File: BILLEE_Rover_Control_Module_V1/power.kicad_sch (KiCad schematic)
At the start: 12 parts, among them CN1 LOGIC_PWR_XT60, U10 LT8612EUDE#TRPBF, U11 LT8612EUDE#TRPBF, U12 JETSON_PWR, U13 JETSON_PWR, U14 JETSON_PWR, U5 INA780BIDEKR, U6 TPS1HA08BQPWPRQ1, U7 TPS1HA08BQPWPRQ1, U8 TPS1HA08BQPWPRQ1, U9 LT8612EUDE#TRPBF

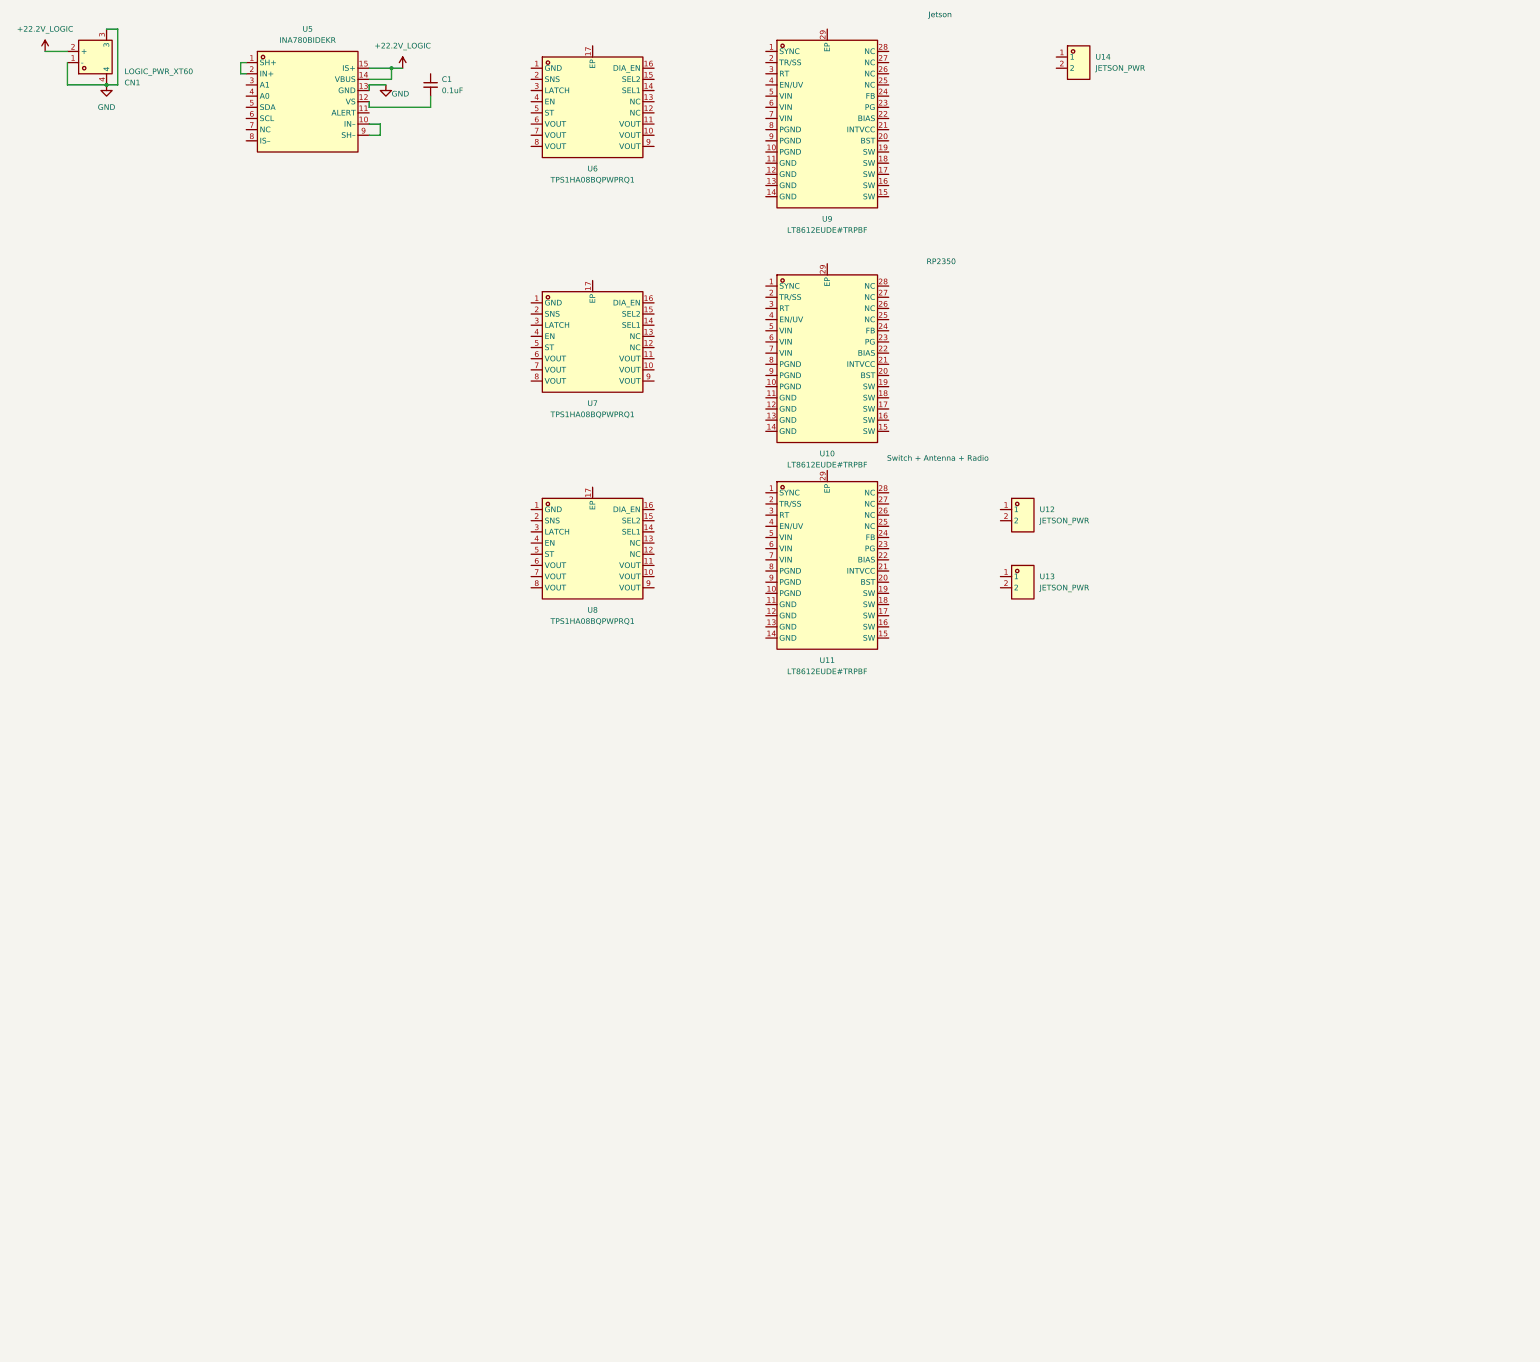
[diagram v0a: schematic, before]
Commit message: Implemented Logic Subsystem
Implemented all of the Logic subsystem, missing reverse circuit protection.
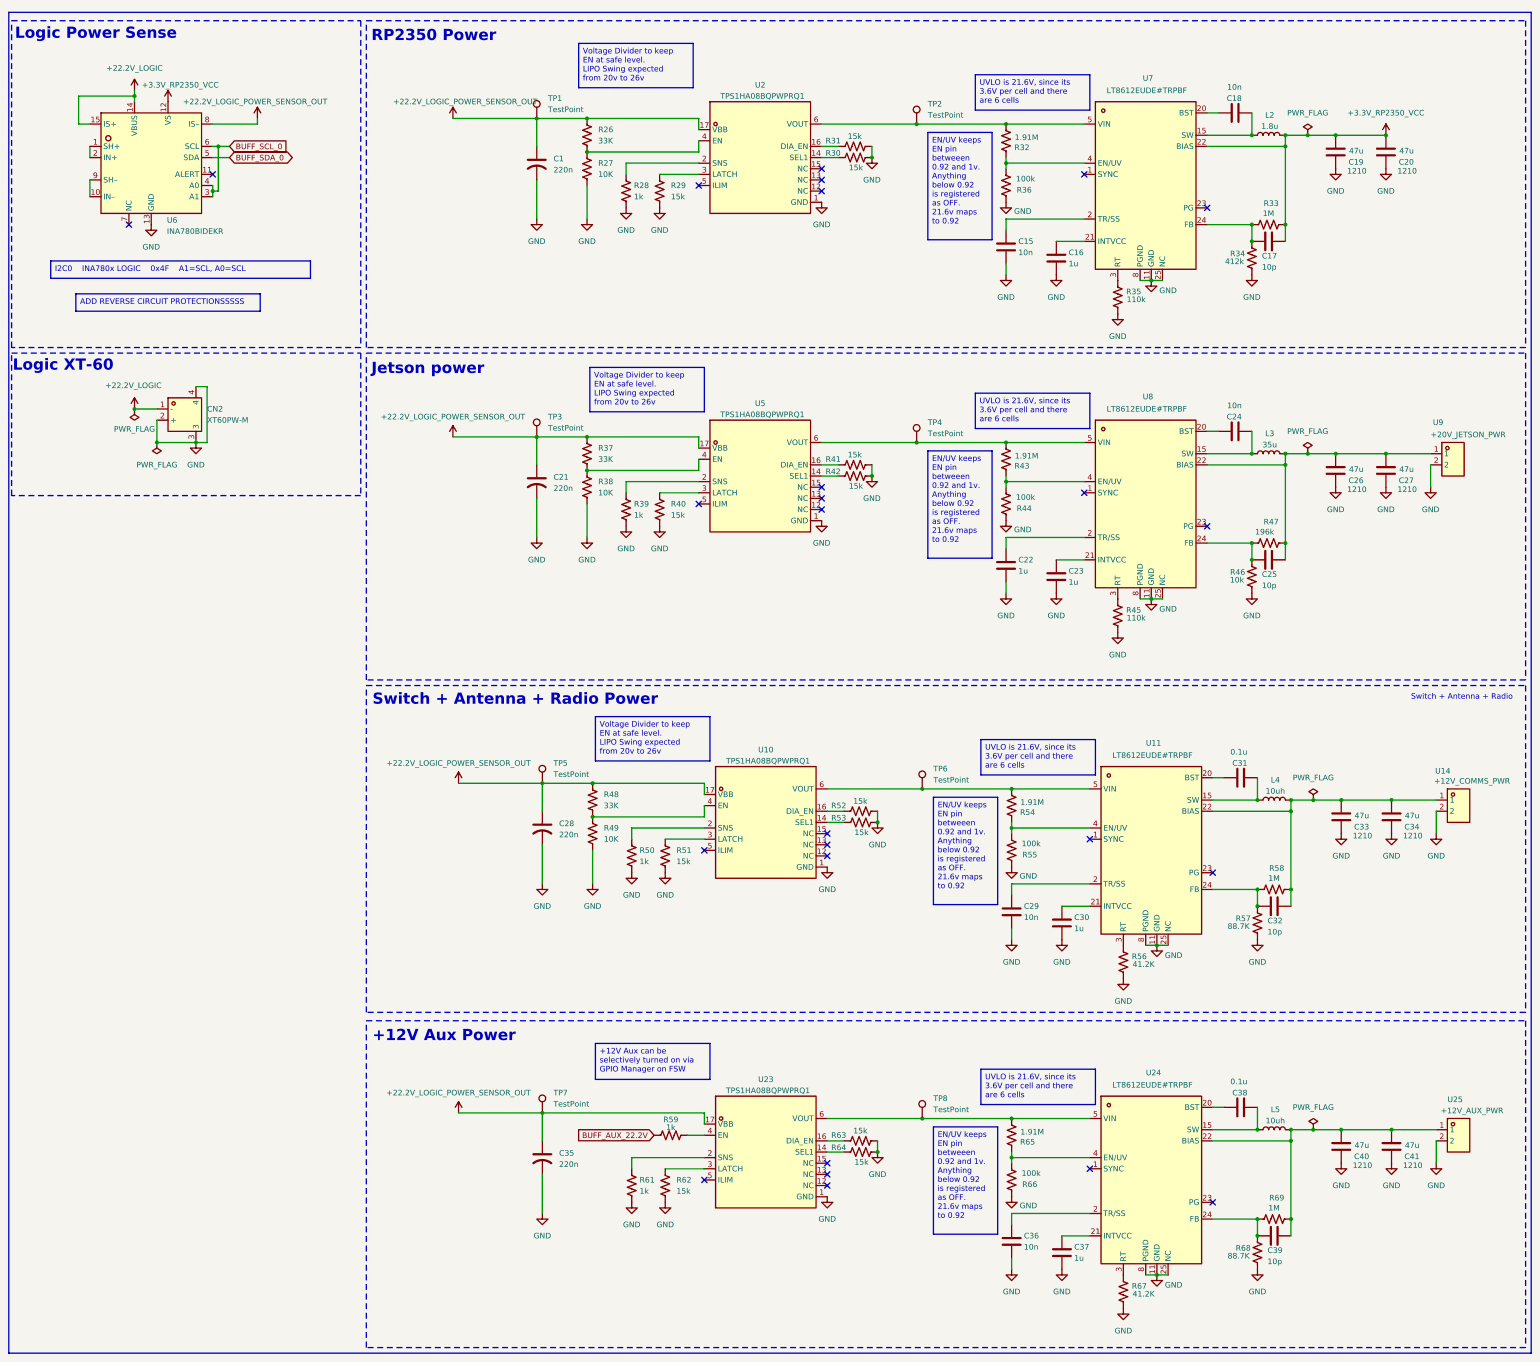
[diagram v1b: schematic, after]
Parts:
- removed C1: 0.1uF, symbol Device:C_Small
- removed CN1: LOGIC_PWR_XT60, PDB_LCSC:CONN-TH_XT60PW-M, symbol PDB_LSCS_Libs:XT60PW-M
- removed U10, U11, U9: LT8612EUDE#TRPBF, PDB_LCSC:QFN-28_L6.0-W3.0-P0.50-BL-EP, symbol PDB_LSCS_Libs:LT8612EUDE#TRPBF
- removed U12, U13, U14: JETSON_PWR, PDB_LCSC:CONN-TH_P5.00_KF301-5.0-2P, symbol PDB_LSCS_Libs:KF301-5.0-2P
- removed U5: INA780BIDEKR, PDB_LCSC:VQFN-15_L6.0-W6.0-P0.60-TL, symbol PDB_LSCS_Libs:INA780BIDEKR
- removed U6, U7, U8: TPS1HA08BQPWPRQ1, PDB_LCSC:HTSSOP-16_L5.0-W4.4-P0.65-LS6.4-BL-EP, symbol PDB_LSCS_Libs:TPS1HA08BQPWPRQ1
- added C1, C21, C28, C35: 220n, symbol Device:C_US
- added C15, C18, C24, C29, C36: 10n, symbol Device:C
- added C16, C22, C23, C30, C37: 1u, symbol Device:C
- added C17, C25, C32, C39: 10p, symbol Device:C
- added C19, C20, C26, C27, C33, C34, C40, C41: 47u, symbol Device:C
- added C31, C38: 0.1u, symbol Device:C
- added CN2: XT60PW-M, PDB_LCSC:CONN-TH_XT60PW-M, symbol PDB_LCSC_Libs:XT60PW-M
- added L2: 1.8u, symbol Device:L
- added L3: 35u, symbol Device:L
- added L4, L5: 10uh, symbol Device:L
- added R26, R37, R48: 33K, symbol Device:R_US
- added R27, R38, R49: 10K, symbol Device:R_US
- added R28, R39, R50, R59, R61: 1k, symbol Device:R_US
- added R29, R30, R31, R40, R41, R42, R51, R52, R53, R62, R63, R64: 15k, symbol Device:R_US
- added R32, R43, R54, R65: 1.91M, symbol Device:R_US
- added R33, R58, R69: 1M, symbol Device:R_US
- added R34: 412k, symbol Device:R_US
- added R35, R45: 110k, symbol Device:R_US
- added R36, R44, R55, R66: 100k, symbol Device:R_US
- added R46: 10k, symbol Device:R_US
- added R47: 196k, symbol Device:R_US
- added R56, R67: 41.2K, symbol Device:R_US
- added R57, R68: 88.7K, symbol Device:R_US
- added TP1, TP2, TP3, TP4, TP5, TP6, TP7, TP8: TestPoint, Connector_Pin:Pin_D1.0mm_L10.0mm, symbol Connector:TestPoint
- added U10, U2, U23, U5: TPS1HA08BQPWPRQ1, PDB_LCSC:HTSSOP-16_L5.0-W4.4-P0.65-LS6.4-BL-EP, symbol PDB_LCSC_Libs:TPS1HA08BQPWPRQ1
- added U11, U24, U7, U8: LT8612EUDE#TRPBF, PDB_LCSC:QFN-28_L6.0-W3.0-P0.50-BL-EP, symbol PDB_LCSC_Libs:LT8612EUDE#TRPBF
- added U14: +12V_COMMS_PWR, PDB_LCSC:CONN-TH_P5.00_KF301-5.0-2P, symbol PDB_LCSC_Libs:KF301-5.0-2P
- added U25: +12V_AUX_PWR, PDB_LCSC:CONN-TH_P5.00_KF301-5.0-2P, symbol PDB_LCSC_Libs:KF301-5.0-2P
- added U6: INA780BIDEKR, PDB_LCSC:VQFN-15_L6.0-W6.0-P0.60-TL, symbol PDB_LCSC_Libs:INA780BIDEKR
- added U9: +20V_JETSON_PWR, PDB_LCSC:CONN-TH_P5.00_KF301-5.0-2P, symbol PDB_LCSC_Libs:KF301-5.0-2P
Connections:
- net +22.2V_LOGIC: now also CN2.1 (-), U6.14 (VBUS), U6.15 (IS+)
- net GND: now also C1.2, C15.2, C16.2, C19.2, C20.2, C21.2, C22.2, C23.2, C26.2, C27.2, C28.2, C29.2, C30.2, C33.2, C34.2, C35.2, C36.2, C37.2, C40.2, C41.2, CN2.2 (+), CN2.3, CN2.4, R27.2, R28.2, R29.2, R30.2, R31.2, R34.2, R35.1, R36.1, R38.2, R39.2, R40.2, R41.2, R42.2, R44.1, R45.1, R46.2, R49.2, R50.2, R51.2, R52.2, R53.2, R55.1, R56.1, R57.2, R61.2, R62.2, R63.2, R64.2, R66.1, R67.1, R68.2, U10.1 (GND), U11.11 (GND), U11.25 (NC), U11.8 (PGND), U14.2, U2.1 (GND), U23.1 (GND), U24.11 (GND), U24.25 (NC), U24.8 (PGND), U25.2, U5.1 (GND), U6.13 (GND), U7.11 (GND), U7.25 (NC), U7.8 (PGND), U8.11 (GND), U8.25 (NC), U8.8 (PGND), U9.2
- new net: R65.1, R66.2, U24.4 (EN/UV)
- new net: R41.1, U5.16 (DIA_EN)
- new net: R35.2, U7.3 (RT)
- new net: R26.2, R27.1, U2.4 (EN)
- new net: C38.1, U24.20 (BST)
- new net: C38.2, L5.1, U24.15 (SW)
- new net: C37.1, U24.21 (INTVCC)
- new net: C25.2, R46.1, R47.2, U8.24 (FB)
- new net: C39.1, C40.1, C41.1, L5.2, R69.1, U24.22 (BIAS), U25.1
- new net: C32.1, C33.1, C34.1, L4.2, R58.1, U11.22 (BIAS), U14.1
- new net: C36.1, U24.2 (TR/SS)
- new net: C39.2, R68.1, R69.2, U24.24 (FB)
- new net: R67.2, U24.3 (RT)
- new net: R65.2, TP8.1, U23.6 (VOUT), U24.5 (VIN)
- new net: R30.1, U2.14 (SEL1)
- new net: R31.1, U2.16 (DIA_EN)
- new net: R28.1, U2.2 (SNS)
- new net: R29.1, U2.3 (LATCH)
- new net: R32.2, TP2.1, U2.6 (VOUT), U7.5 (VIN)
- new net: R54.1, R55.2, U11.4 (EN/UV)
- new net: R54.2, TP6.1, U10.6 (VOUT), U11.5 (VIN)
- new net: C18.2, L2.1, U7.15 (SW)
- new net: C25.1, C26.1, C27.1, L3.2, R47.1, U8.22 (BIAS), U9.1
- new net: R43.2, TP4.1, U5.6 (VOUT), U8.5 (VIN)
- new net: R37.2, R38.1, U5.4 (EN)
- new net: R45.2, U8.3 (RT)
- new net: C17.2, R33.2, R34.1, U7.24 (FB)
- new net: R43.1, R44.2, U8.4 (EN/UV)
- new net: C30.1, U11.21 (INTVCC)
- new net: R48.2, R49.1, U10.4 (EN)
- new net: C32.2, R57.1, R58.2, U11.24 (FB)
- new net: R32.1, R36.2, U7.4 (EN/UV)
- new net: R51.1, U10.3 (LATCH)
- new net: C31.2, L4.1, U11.15 (SW)
- new net: R42.1, U5.14 (SEL1)
- new net: R39.1, U5.2 (SNS)
- new net: R40.1, U5.3 (LATCH)
- new net: R50.1, U10.2 (SNS)
- new net: C29.1, U11.2 (TR/SS)
- new net: C31.1, U11.20 (BST)
- new net: R56.2, U11.3 (RT)
- new net: R53.1, U10.14 (SEL1)
- new net: C22.1, U8.2 (TR/SS)
- new net: R64.1, U23.14 (SEL1)
- new net: R63.1, U23.16 (DIA_EN)
- new net: R61.1, U23.2 (SNS)
- new net: R62.1, U23.3 (LATCH)
- new net: R59.2, U23.4 (EN)
- new net: C15.1, U7.2 (TR/SS)
- new net: C18.1, U7.20 (BST)
- new net: C16.1, U7.21 (INTVCC)
- new net: R52.1, U10.16 (DIA_EN)
- new net: C24.2, L3.1, U8.15 (SW)
- new net: C24.1, U8.20 (BST)
- new net: C23.1, U8.21 (INTVCC)
- new net: U6.1 (SH+), U6.2 (IN+)
- new net: U6.10 (IN–), U6.9 (SH–)
- new net +22.2V_LOGIC_POWER_SENSOR_OUT: C1.1, C21.1, C28.1, C35.1, R26.1, R37.1, R48.1, TP1.1, TP3.1, TP5.1, TP7.1, U10.17 (VBB), U2.17 (VBB), U23.17 (VBB), U5.17 (VBB), U6.8 (IS–)
- new net +3.3V_RP2350_VCC: C17.1, C19.1, C20.1, L2.2, R33.1, U6.12 (VS), U7.22 (BIAS)
- new net BUFF_AUX_22.2V: R59.1
- new net BUFF_SCL_0: U6.3 (A1), U6.4 (A0), U6.6 (SCL)
- new net BUFF_SDA_0: U6.5 (SDA)
- no-connect marks 0 -> 26
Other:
- note added: "+12V Aux Power"
- note added: "Jetson power"
- note added: "Logic Power Sense"
- note added: "Logic XT-60"
- note added: "RP2350 Power"
- note added: "Switch + Antenna + Radio Power"
- note removed: "Jetson"
- note removed: "RP2350"

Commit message: WIP Checkpoint
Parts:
- removed C28: 220n, symbol Device:C_US
- removed C29: 10n, symbol Device:C
- removed C30: 1u, symbol Device:C
- removed C31: 0.1u, symbol Device:C
- removed C32: 10p, symbol Device:C
- removed C33, C34: 47u, symbol Device:C
- removed L4: 10uh, symbol Device:L
- removed R48: 33K, symbol Device:R_US
- removed R49: 10K, symbol Device:R_US
- removed R50: 1k, symbol Device:R_US
- removed R51, R52, R53: 15k, symbol Device:R_US
- removed R54: 1.91M, symbol Device:R_US
- removed R55: 100k, symbol Device:R_US
- removed R56: 41.2K, symbol Device:R_US
- removed R57: 88.7K, symbol Device:R_US
- removed R58: 1M, symbol Device:R_US
- removed TP5, TP6: TestPoint, Connector_Pin:Pin_D1.0mm_L10.0mm, symbol Connector:TestPoint
- removed U10: TPS1HA08BQPWPRQ1, PDB_LCSC:HTSSOP-16_L5.0-W4.4-P0.65-LS6.4-BL-EP, symbol PDB_LCSC_Libs:TPS1HA08BQPWPRQ1
- removed U11: LT8612EUDE#TRPBF, PDB_LCSC:QFN-28_L6.0-W3.0-P0.50-BL-EP, symbol PDB_LCSC_Libs:LT8612EUDE#TRPBF
- removed U14: +12V_COMMS_PWR, PDB_LCSC:CONN-TH_P5.00_KF301-5.0-2P, symbol PDB_LCSC_Libs:KF301-5.0-2P
- added R72: 10K, symbol Device:R_US
- added U10: +22.2V_POE_POWER, PDB_LCSC:CONN-TH_P5.00_KF301-5.0-2P, symbol PDB_LCSC_Libs:KF301-5.0-2P
- added U20: +12V_NET_SW_PWR, PDB_LCSC:CONN-TH_P5.00_KF301-5.0-2P, symbol PDB_LCSC_Libs:KF301-5.0-2P
- added U38: MCP9808T-E/MS, PDB_LCSC:MSOP-8_L3.0-W3.0-P0.65-LS4.9-BL, symbol PDB_LCSC_Libs:MCP9808T-E_MS
- C1, C21, C35: symbol Device:C_US -> Device:C
- R59: value 1k -> 33K
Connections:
- net BUFF_AUX_22.2V is gone; now on net +22.2V_LOGIC_POWER_SENSOR_OUT: R59.1
- net +22.2V_LOGIC: now also CN2.2 (+); no longer CN2.1 (-)
- net GND: now also CN2.1 (-), R72.2, U10.2, U20.2; no longer CN2.2 (+)
- net +12V_AUX_VCC: now reaches C39.1, C40.1, C41.1, L5.2, R69.1, U24.22 (BIAS), U25.1
- net +12V_AUX_VCC: now also U20.1
- net +20V_JETSON_VCC: now reaches C25.1, C26.1, C27.1, L3.2, R47.1, U8.22 (BIAS), U9.1
- net +22.2V_POE_VCC: now reaches R43.2, TP4.1, U5.6 (VOUT), U8.5 (VIN)
- net +22.2V_POE_VCC: now also U10.1
- net at R59.2, U23.4 (EN): now also R72.1
- no-connect marks 26 -> 20
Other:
- note added: "(+22.2v -> +20v) Jetson power + POE"
- note added: "(+22.2v -> +3.3v) RP2350 Power"
- note added: "+12V Network Switch and Aux Power"
- note added: "Logic Temp Sense"
- note removed: "+12V Aux Power"
- note removed: "Jetson power"
- note removed: "RP2350 Power"
- note removed: "Switch + Antenna + Radio"
- note removed: "Switch + Antenna + Radio Power"
- moved on the sheet: C21, C22, C23, C24, C25, C26, C27, C35, C36, C37, C38, C39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

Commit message: Goodies
Updated all schematics
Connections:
- net +3.3V_RP2350_VCC: now also U38.8 (VDD)
- net GND: now also U38.4 (GND), U38.5 (A2), U38.6 (A1), U38.7 (A0)
- net BUFF_SDA_1: now reaches U38.1 (SDA)
- net BUFF_SCL_1: now reaches U38.2 (SCL)
- no-connect marks 20 -> 21
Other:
- company: (none) -> Bronco STAR
- title: (none) -> BILLEE_RCM
- moved on the sheet: U38, U6

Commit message: more goodies
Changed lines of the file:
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@@
 	(generator "eeschema")
 	(generator_version "10.0")
-	(paper "A2")
+	(paper "A3")
 	(title_block
 		(title "BILLEE_RCM")
@@
 	(rectangle
 		(start 13.335 13.97)
-		(end 359.41 318.77)
+		(end 359.41 244.475)
 		(stroke
 			(width 0)
